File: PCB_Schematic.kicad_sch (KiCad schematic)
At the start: 11 parts, among them J4 Conn_01x02_Pin, U6 STM32F091RCTx

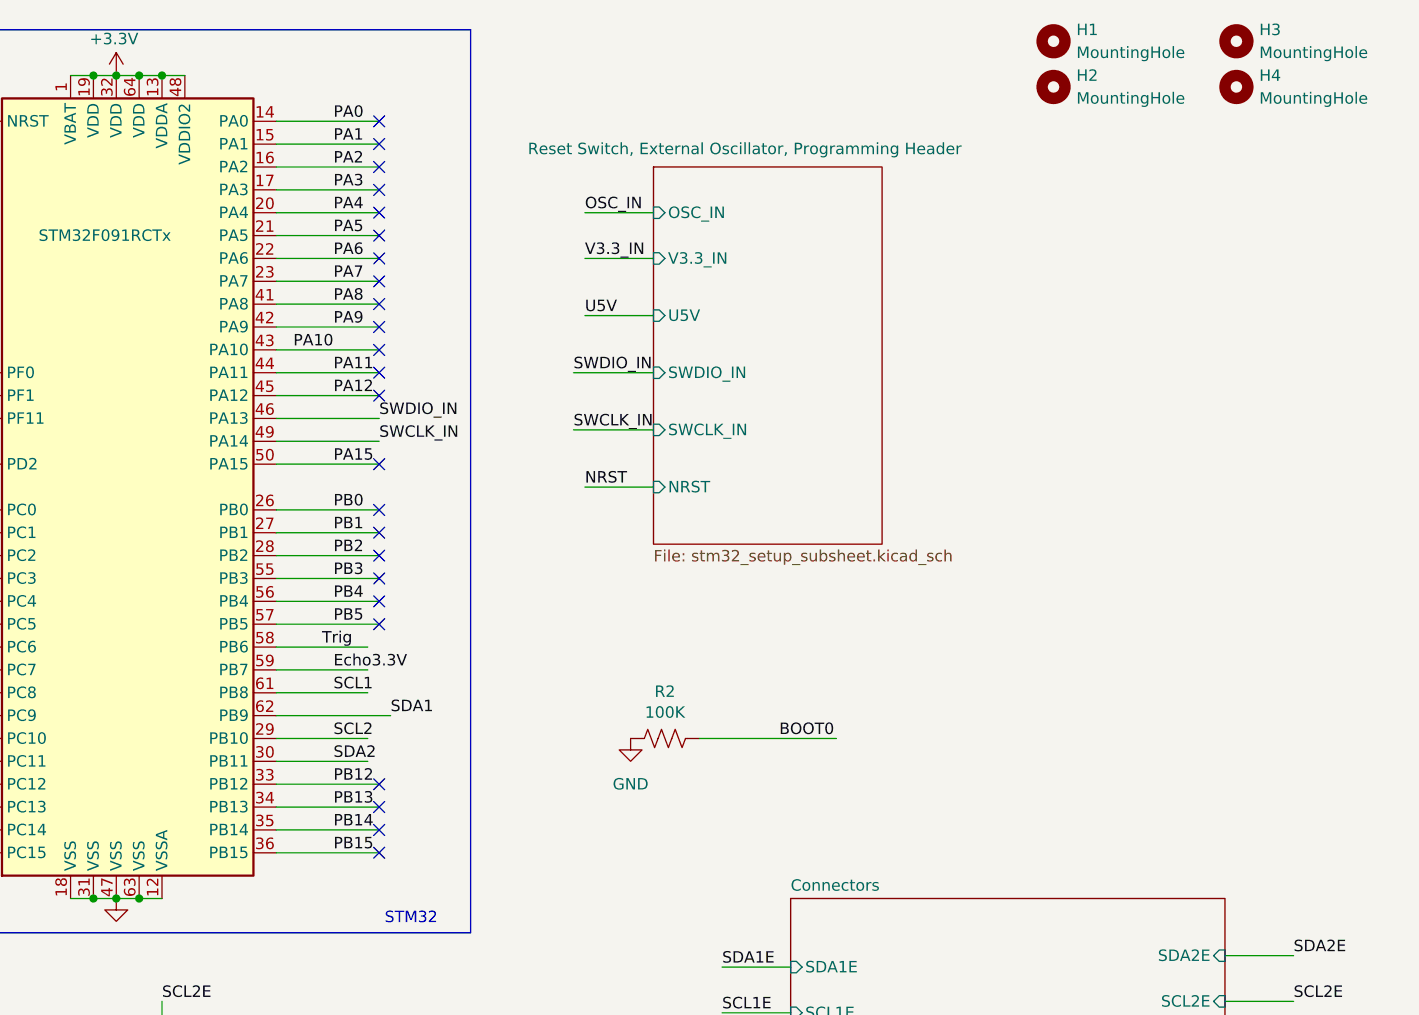
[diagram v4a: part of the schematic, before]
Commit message: remove un-needed program header circuitry, add debug LEDs, add USB ESD, add shcotty for LM117
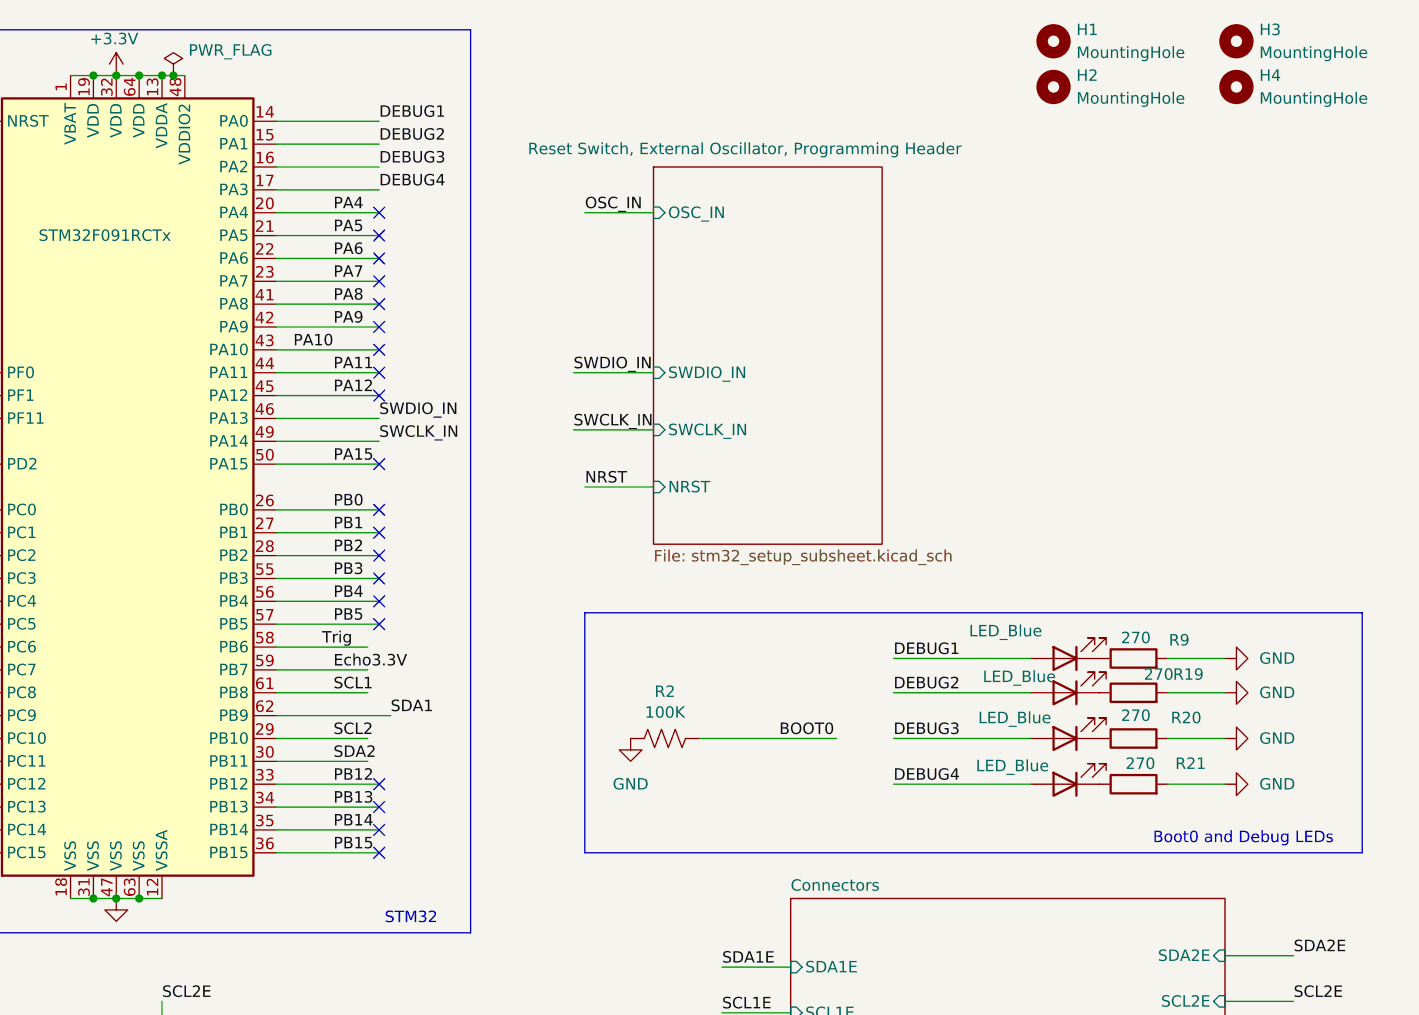
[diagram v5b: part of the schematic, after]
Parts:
- added D17, D18, D19, D7: LED_Blue, LED_SMD:LED_0805_2012Metric_Pad1.15x1.40mm_HandSolder, symbol Device:LED
- added R19, R20, R21, R9: 270, Capacitor_SMD:C_0805_2012Metric_Pad1.18x1.45mm_HandSolder, symbol Device:R
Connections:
- net GND: now also R19.2, R20.2, R21.2, R9.2
- net PA0 renamed DEBUG1
- net DEBUG1: now also D7.2 (A)
- net PA1 renamed DEBUG2
- net DEBUG2: now also D17.2 (A)
- net PA2 renamed DEBUG3
- net DEBUG3: now also D18.2 (A)
- net PA3 renamed DEBUG4
- net DEBUG4: now also D19.2 (A)
- new net: D18.1 (K), R20.1
- new net: D19.1 (K), R21.1
- new net: D7.1 (K), R9.1
- new net: D17.1 (K), R19.1
- no-connect marks 38 -> 34
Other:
- sheet Reset Switch, External Oscillator, Programming Header ports: added none; removed U5V, V3.3_IN
- note added: "Boot0 and Debug LEDs"

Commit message: starter PCB
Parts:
- renumbered D6 to D1, D5 to D2, D7 to D3, D17 to D4, D18 to D5, D19 to D6, J4 to J1, R10 to R1, R7 to R2, R2 to R3, R9 to R4, R19 to R5, R20 to R6, R21 to R7, U6 to U1
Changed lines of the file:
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@@
 		(dnp no)
 		(fields_autoplaced yes)
-		(property "Reference" "#PWR034"
+		(property "Reference" "#PWR03"
 			(at 87.63 105.41 0)
 			(effects
@@
 			(project "PCB_Schematic"
 				(path "/a0c17764-e0d1-4df5-b871-1489cf266494"
-					(reference "#PWR034")
+					(reference "#PWR03")
 					(unit 1)
 				)
@@
 		(on_board yes)
 		(dnp no)
-		(property "Reference" "R20"
+		(property "Reference" "R6"
 			(at 261.112 91.694 90)
 			(effects
@@
 			(project "PCB_Schematic"
 				(path "/a0c17764-e0d1-4df5-b871-1489cf266494"
-					(reference "R20")
+					(reference "R6")
 					(unit 1)
 				)
@@
 		(on_board yes)
 		(dnp no)
-		(property "Reference" "#PWR019"
+		(property "Reference" "#PWR01"
 			(at 55.88 105.41 0)
 			(effects
@@
 			(project "PCB_Schematic"
 				(path "/a0c17764-e0d1-4df5-b871-1489cf266494"
-					(reference "#PWR019")
+					(reference "#PWR01")
 					(unit 1)
 				)
@@
 		(on_board yes)
 		(dnp no)
-		(property "Reference" "R10"
+		(property "Reference" "R1"
 			(at 68.58 100.33 90)
 			(effects
@@
 			(project "PCB_Schematic"
 				(path "/a0c17764-e0d1-4df5-b871-1489cf266494"
-					(reference "R10")
+					(reference "R1")
 					(unit 1)
 				)
@@
 		(on_board yes)
 		(dnp no)
-		(property "Reference" "R7"
+		(property "Reference" "R2"
 			(at 68.58 110.49 90)
 			(effects
@@
 			(project "PCB_Schematic"
 				(path "/a0c17764-e0d1-4df5-b871-1489cf266494"
-					(reference "R7")
+					(reference "R2")
 					(unit 1)
 				)
@@
 		(on_board yes)
 		(dnp no)
-		(property "Reference" "D19"
+		(property "Reference" "D6"
 			(at 249.2375 91.44 0)
 			(effects
@@
 			(project "PCB_Schematic"
 				(path "/a0c17764-e0d1-4df5-b871-1489cf266494"
-					(reference "D19")
+					(reference "D6")
 					(unit 1)
 				)
@@
 		(dnp no)
 		(fields_autoplaced yes)
-		(property "Reference" "#PWR016"
+		(property "Reference" "#PWR07"
 			(at 199.39 100.33 0)
 			(effects
@@
 			(project "PCB_Schematic"
 				(path "/a0c17764-e0d1-4df5-b871-1489cf266494"
-					(reference "#PWR016")
+					(reference "#PWR07")
 					(unit 1)
 				)
@@
 		(on_board yes)
 		(dnp no)
-		(property "Reference" "U6"
+		(property "Reference" "U1"
 			(at 125.73 38.1 0)
 			(effects
@@
 			(project ""
 				(path "/a0c17764-e0d1-4df5-b871-1489cf266494"
-					(reference "U6")
+					(reference "U1")
 					(unit 1)
 				)
@@
 		(on_board yes)
 		(dnp no)
-		(property "Reference" "D18"
+		(property "Reference" "D5"
 			(at 249.2375 86.36 0)
 			(effects
@@
 			(project "PCB_Schematic"
 				(path "/a0c17764-e0d1-4df5-b871-1489cf266494"
-					(reference "D18")
+					(reference "D5")
 					(unit 1)
 				)
@@
 		(on_board yes)
 		(dnp no)
-		(property "Reference" "R9"
+		(property "Reference" "R4"
 			(at 260.35 83.058 90)
 			(effects
@@
 			(project "PCB_Schematic"
 				(path "/a0c17764-e0d1-4df5-b871-1489cf266494"
-					(reference "R9")
+					(reference "R4")
 					(unit 1)
 				)
@@
 		(dnp no)
 		(fields_autoplaced yes)
-		(property "Reference" "#PWR030"
+		(property "Reference" "#PWR09"
 			(at 271.78 88.9 0)
 			(effects
@@
 			(project ""
 				(path "/a0c17764-e0d1-4df5-b871-1489cf266494"
-					(reference "#PWR030")
+					(reference "#PWR09")
 					(unit 1)
 				)
@@
 		(dnp no)
 		(fields_autoplaced yes)
-		(property "Reference" "#PWR029"
+		(property "Reference" "#PWR08"
 			(at 271.78 85.09 0)
 			(effects
@@
 			(project ""
 				(path "/a0c17764-e0d1-4df5-b871-1489cf266494"
-					(reference "#PWR029")
+					(reference "#PWR08")
 					(unit 1)
 				)
@@
 		(dnp no)
 		(fields_autoplaced yes)
-		(property "Reference" "#PWR025"
+		(property "Reference" "#PWR04"
 			(at 87.63 115.57 0)
 			(effects
@@
 			(project "PCB_Schematic"
 				(path "/a0c17764-e0d1-4df5-b871-1489cf266494"
-					(reference "#PWR025")
+					(reference "#PWR04")
 					(unit 1)
 				)
@@
 		(on_board yes)
 		(dnp no)
-		(property "Reference" "R21"
+		(property "Reference" "R7"
 			(at 261.62 96.774 90)
 			(effects
@@
 			(project "PCB_Schematic"
 				(path "/a0c17764-e0d1-4df5-b871-1489cf266494"
-					(reference "R21")
+					(reference "R7")
 					(unit 1)
 				)
@@
 		(dnp no)
 		(fields_autoplaced yes)
-		(property "Reference" "#PWR032"
+		(property "Reference" "#PWR011"
 			(at 271.78 99.06 0)
 			(effects
@@
 			(project ""
 				(path "/a0c17764-e0d1-4df5-b871-1489cf266494"
-					(reference "#PWR032")
+					(reference "#PWR011")
 					(unit 1)
 				)
@@
 		(dnp no)
 		(fields_autoplaced yes)
-		(property "Reference" "#PWR024"
+		(property "Reference" "#PWR02"
 			(at 55.88 115.57 0)
 			(effects
@@
 			(project ""
 				(path "/a0c17764-e0d1-4df5-b871-1489cf266494"
-					(reference "#PWR024")
+					(reference "#PWR02")
 					(unit 1)
 				)
@@
 		(on_board yes)
 		(dnp no)
-		(property "Reference" "D7"
+		(property "Reference" "D3"
 			(at 249.2375 77.47 0)
 			(effects
@@
 			(project "PCB_Schematic"
 				(path "/a0c17764-e0d1-4df5-b871-1489cf266494"
-					(reference "D7")
+					(reference "D3")
 					(unit 1)
 				)
@@
 		(on_board yes)
 		(dnp no)
-		(property "Reference" "D17"
+		(property "Reference" "D4"
 			(at 249.2375 81.28 0)
 			(effects
@@
 			(project "PCB_Schematic"
 				(path "/a0c17764-e0d1-4df5-b871-1489cf266494"
-					(reference "D17")
+					(reference "D4")
 					(unit 1)
 				)
@@
 		(dnp no)
 		(fields_autoplaced yes)
-		(property "Reference" "J4"
+		(property "Reference" "J1"
 			(at 27.305 100.33 0)
 			(effects
@@
 			(project ""
 				(path "/a0c17764-e0d1-4df5-b871-1489cf266494"
-					(reference "J4")
+					(reference "J1")
 					(unit 1)
 				)
@@
 		(on_board yes)
 		(dnp no)
-		(property "Reference" "R2"
+		(property "Reference" "R3"
 			(at 203.2 88.773 90)
 			(effects
@@
 			(project "PCB_Schematic"
 				(path "/a0c17764-e0d1-4df5-b871-1489cf266494"
-					(reference "R2")
+					(reference "R3")
 					(unit 1)
 				)
@@
 		(on_board yes)
 		(dnp no)
-		(property "Reference" "#PWR02"
+		(property "Reference" "#PWR05"
 			(at 142.24 24.13 0)
 			(effects
@@
 			(project ""
 				(path "/a0c17764-e0d1-4df5-b871-1489cf266494"
-					(reference "#PWR02")
+					(reference "#PWR05")
 					(unit 1)
 				)
@@
 		(dnp no)
 		(fields_autoplaced yes)
-		(property "Reference" "#PWR031"
+		(property "Reference" "#PWR010"
 			(at 271.78 93.98 0)
 			(effects
@@
 			(project ""
 				(path "/a0c17764-e0d1-4df5-b871-1489cf266494"
-					(reference "#PWR031")
+					(reference "#PWR010")
 					(unit 1)
 				)
@@
 		(on_board yes)
 		(dnp no)
-		(property "Reference" "#FLG03"
+		(property "Reference" "#FLG01"
 			(at 148.59 18.415 0)
 			(effects
@@
 			(project ""
 				(path "/a0c17764-e0d1-4df5-b871-1489cf266494"
-					(reference "#FLG03")
+					(reference "#FLG01")
 					(unit 1)
 				)
@@
 		(dnp no)
 		(fields_autoplaced yes)
-		(property "Reference" "D5"
+		(property "Reference" "D2"
 			(at 77.7875 107.95 0)
 			(effects
@@
 			(project "PCB_Schematic"
 				(path "/a0c17764-e0d1-4df5-b871-1489cf266494"
-					(reference "D5")
+					(reference "D2")
 					(unit 1)
 				)
@@
 		(on_board yes)
 		(dnp no)
-		(property "Reference" "#PWR0101"
+		(property "Reference" "#PWR06"
 			(at 142.24 118.11 0)
 			(effects
@@
 			(project ""
 				(path "/a0c17764-e0d1-4df5-b871-1489cf266494"
-					(reference "#PWR0101")
+					(reference "#PWR06")
 					(unit 1)
 				)
@@
 		(dnp no)
 		(fields_autoplaced yes)
-		(property "Reference" "D6"
+		(property "Reference" "D1"
 			(at 77.7875 97.79 0)
 			(effects
@@
 			(project "PCB_Schematic"
 				(path "/a0c17764-e0d1-4df5-b871-1489cf266494"
-					(reference "D6")
+					(reference "D1")
 					(unit 1)
 				)
@@
 		(on_board yes)
 		(dnp no)
-		(property "Reference" "R19"
+		(property "Reference" "R5"
 			(at 261.366 86.868 90)
 			(effects
@@
 			(project "PCB_Schematic"
 				(path "/a0c17764-e0d1-4df5-b871-1489cf266494"
-					(reference "R19")
-					(unit 1)
-				)
+					(reference "R5")
+					(unit 1)
+				)

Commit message: more
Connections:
- net PB12 is gone; now on net DEBUG1: U1.33 (PB12)
- net PB13 is gone; now on net DEBUG2: U1.34 (PB13)
- net PB14 is gone; now on net DEBUG3: U1.35 (PB14)
- net PB15 is gone; now on net DEBUG4: U1.36 (PB15)
- net DEBUG1: no longer U1.14 (PA0)
- net DEBUG2: no longer U1.15 (PA1)
- net DEBUG3: no longer U1.16 (PA2)
- net DEBUG4: no longer U1.17 (PA3)
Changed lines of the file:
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@@
-	)
-	(no_connect
-		(at 171.45 99.06)
 	)
 	(no_connect
@@
 	)
 	(no_connect
-		(at 171.45 106.68)
-	)
-	(no_connect
 		(at 171.45 38.1)
 	)
@@
 	)
 	(no_connect
-		(at 171.45 101.6)
-	)
-	(no_connect
 		(at 171.45 48.26)
 	)
 	(no_connect
+		(at 171.45 30.48)
+	)
+	(no_connect
 		(at 115.57 78.74)
 	)
@@
 	)
 	(no_connect
-		(at 171.45 104.14)
+		(at 171.45 25.4)
 	)
 	(no_connect
@@
 	)
 	(no_connect
+		(at 171.45 27.94)
+	)
+	(no_connect
 		(at 171.45 81.28)
 	)
@@
 	(no_connect
 		(at 171.45 78.74)
+	)
+	(no_connect
+		(at 171.45 33.02)
 	)
 	(wire
@@
 		)
 	)
+	(label "DEBUG3"
+		(at 171.45 104.14 0)
+		(fields_autoplaced yes)
+		(effects
+			(font
+				(size 1.27 1.27)
+			)
+			(justify left bottom)
+		)
+	)
 	(label "USBD+"
 		(at 25.4 36.83 0)
@@
 		)
 	)
-	(label "DEBUG3"
-		(at 171.45 30.48 0)
+	(label "DEBUG1"
+		(at 171.45 99.06 0)
 		(fields_autoplaced yes)
 		(effects
@@
 		)
 	)
-	(label "PB14"
-		(at 166.37 104.14 0)
-		(fields_autoplaced yes)
-		(effects
-			(font
-				(size 1.27 1.27)
-			)
-			(justify left bottom)
-		)
-	)
 	(label "SCL1"
 		(at 114.3 140.97 0)
@@
 		)
 	)
-	(label "DEBUG1"
-		(at 171.45 25.4 0)
-		(fields_autoplaced yes)
-		(effects
-			(font
-				(size 1.27 1.27)
-			)
-			(justify left bottom)
-		)
-	)
 	(label "SDA2E"
 		(at 273.05 118.11 0)
@@
 		)
 	)
-	(label "PB15"
-		(at 166.37 106.68 0)
+	(label "DEBUG4"
+		(at 171.45 106.68 0)
 		(fields_autoplaced yes)
 		(effects
@@
 		)
 	)
-	(label "PB12"
-		(at 166.37 99.06 0)
-		(fields_autoplaced yes)
-		(effects
-			(font
-				(size 1.27 1.27)
-			)
-			(justify left bottom)
-		)
-	)
-	(label "PB13"
-		(at 166.37 101.6 0)
-		(fields_autoplaced yes)
-		(effects
-			(font
-				(size 1.27 1.27)
-			)
-			(justify left bottom)
-		)
-	)
 	(label "DEBUG3"
 		(at 228.6 93.98 0)
@@
 		)
 	)
+	(label "DEBUG2"
+		(at 171.45 101.6 0)
+		(fields_autoplaced yes)
+		(effects
+			(font
+				(size 1.27 1.27)
+			)
+			(justify left bottom)
+		)
+	)
 	(label "SDA1"
 		(at 114.3 147.32 0)
@@
 		)
 	)
-	(label "DEBUG2"
-		(at 171.45 27.94 0)
-		(fields_autoplaced yes)
-		(effects
-			(font
-				(size 1.27 1.27)
-			)
-			(justify left bottom)
-		)
-	)
 	(label "PA7"
 		(at 166.37 43.18 0)
@@
 		(fields_autoplaced yes)
 		(effects
-			(font
-				(size 1.27 1.27)
-			)
-			(justify left bottom)
-		)
-	)
-	(label "DEBUG4"
-		(at 171.45 33.02 0)
-		(fields_autoplaced yes)
-		(effects

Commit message: routing v1
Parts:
- J1: footprint Connector_AMASS:AMASS_XT30PW-M_1x02_P2.50mm_Horizontal -> Library:2Pin
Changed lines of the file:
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@@
 			)
 		)
-		(property "Footprint" "Connector_AMASS:AMASS_XT30PW-M_1x02_P2.50mm_Horizontal"
+		(property "Footprint" "Library:2Pin"
 			(at 26.67 105.41 0)
 			(effects
